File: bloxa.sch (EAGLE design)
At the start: 85 parts, among them CON1 PINHEAD_1X02-2.54, CON7 CON-4P-JST_GH-RA, CON8 CON-4P-JST_GH-RA, IC1 TPD3S014DBVR-SOT23-6, IC2 TJA1051(X)/3-SO8, IC6 MCP9700-SC70-5, Q13 BUK9K6R2-40E,115, Q14 BUK9K6R2-40E,115, Q15 BUK9K6R2-40E,115

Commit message: UPDATES
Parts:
- added U$1: CONNECTION, misc:CONNECTION
- added U$8, U$9: FIDUCIALMOUNT, usb2can_master_lib:FIDUCIALMOUNT
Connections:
- net GNDD: now also U$1.P$2
- net PGND: now also U$1.P$1
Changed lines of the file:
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@@
 <variantdefs>
 <variantdef name="Basic"/>
-<variantdef name="nocaps" current="yes"/>
+<variantdef name="nocaps"/>
 </variantdefs>
 <classes>
@@
 <part name="GND6" library="supply_symbols" library_urn="urn:adsk.eagle:library:5017758" deviceset="PGND" device="" value="PGND"/>
 <part name="C1" library="C_digikey" library_urn="urn:adsk.eagle:library:2539367" deviceset="0.1µF" device="-0402" package3d_urn="urn:adsk.eagle:package:2539379/2" technology="-16V_10%_X7R" value="0.1µF"/>
+<part name="U$1" library="misc" library_urn="urn:adsk.eagle:library:5347860" deviceset="CONNECTION" device=""/>
+<part name="GND7" library="supply_symbols" library_urn="urn:adsk.eagle:library:5017758" deviceset="GNDD" device="" value="GNDD"/>
+<part name="GND8" library="supply_symbols" library_urn="urn:adsk.eagle:library:5017758" deviceset="PGND" device="" value="PGND"/>
+<part name="U$8" library="usb2can_master_lib" deviceset="FIDUCIALMOUNT" device="">
+<variant name="Basic" populate="no"/>
+</part>
+<part name="U$9" library="usb2can_master_lib" deviceset="FIDUCIALMOUNT" device="">
+<variant name="Basic" populate="no"/>
+</part>
 </parts>
 <sheets>
@@
 <attribute name="VOLTAGE" x="162.814" y="180.594" size="0.762" layer="96" rot="R270" align="bottom-center"/>
 </instance>
+<instance part="U$1" gate="G$1" x="337.82" y="144.78" smashed="yes"/>
+<instance part="GND7" gate="G$1" x="342.9" y="139.7" smashed="yes">
+<attribute name="VALUE" x="342.9" y="137.668" size="1.27" layer="96" font="vector" ratio="15" align="center"/>
+</instance>
+<instance part="GND8" gate="G$1" x="332.74" y="139.7" smashed="yes" rot="MR0">
+<attribute name="VALUE" x="332.74" y="138.43" size="1.27" layer="97" font="vector" ratio="15" rot="MR0" align="center"/>
+</instance>
+<instance part="U$8" gate="G$1" x="25.4" y="12.7" smashed="yes" rot="R270"/>
+<instance part="U$9" gate="G$1" x="15.24" y="22.86" smashed="yes" rot="R270"/>
 </instances>
 <busses>
@@
 <wire x1="345.44" y1="71.12" x2="345.44" y2="73.66" width="0.1524" layer="91"/>
 <pinref part="GND19" gate="G$1" pin="GNDD"/>
+</segment>
+<segment>
+<pinref part="GND7" gate="G$1" pin="GNDD"/>
+<wire x1="342.9" y1="142.24" x2="342.9" y2="144.78" width="0.1524" layer="91"/>
+<pinref part="U$1" gate="G$1" pin="P$2"/>
+<wire x1="342.9" y1="144.78" x2="340.36" y2="144.78" width="0.1524" layer="91"/>
 </segment>
 </net>
@@
 <pinref part="GND6" gate="G$1" pin="PGND"/>
 </segment>
-</net>
+<segment>
+<pinref part="GND8" gate="G$1" pin="PGND"/>
+<wire x1="332.74" y1="142.24" x2="332.74" y2="144.78" width="0.1524" layer="91"/>
+<pinref part="U$1" gate="G$1" pin="P$1"/>
+<wire x1="332.74" y1="144.78" x2="335.28" y2="144.78" width="0.1524" layer="91"/>
+</segment>
+</net>

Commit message: More polygones updates
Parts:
- added U$3: CONNECTION, misc:CONNECTION
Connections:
- net GND: now also C1.2, C11.2, C3.2, CON1.1, IC2.GND, U$1.P$1, U$3.P$1
- net PGND: now also U$3.P$2; no longer C1.2, C11.2, C3.2, CON1.1, IC2.GND, U$1.P$1
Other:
- moved on the sheet: CON8, LED1, LED3, R11, R12, R13, R9

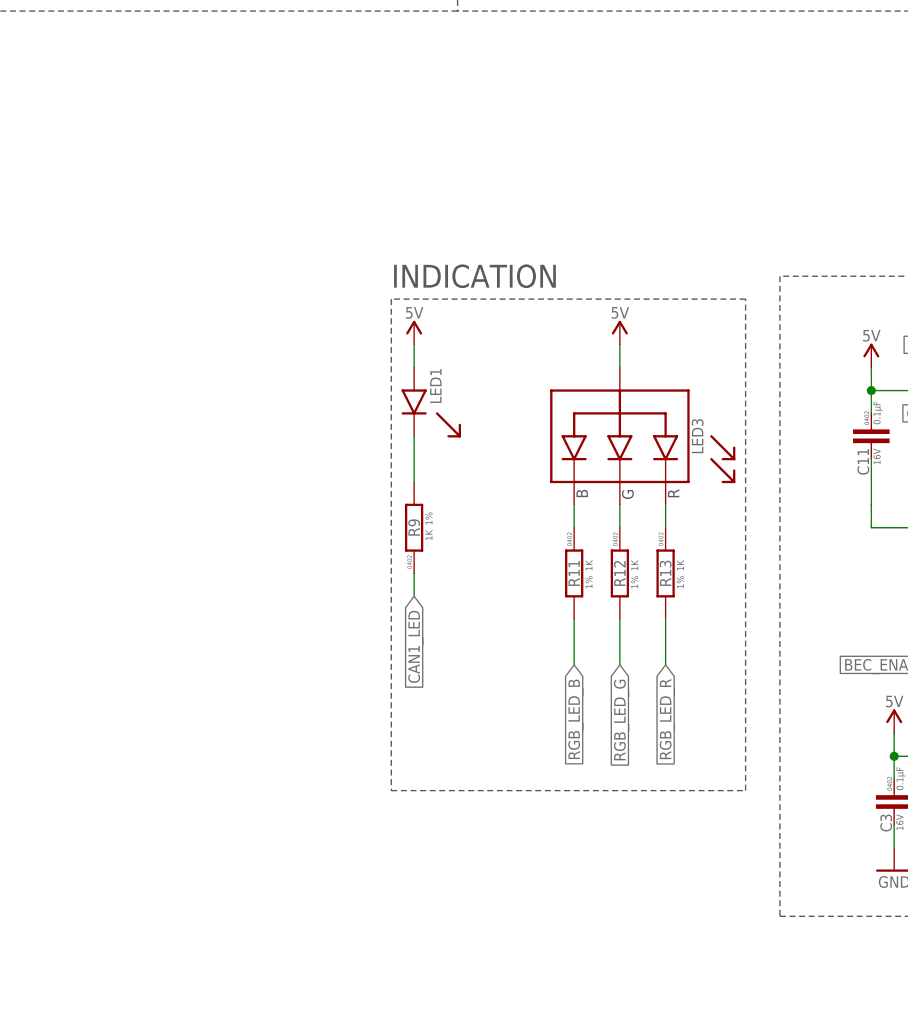
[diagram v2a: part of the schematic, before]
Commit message: alternate footprints for LED fancy placement
Will never use it probably
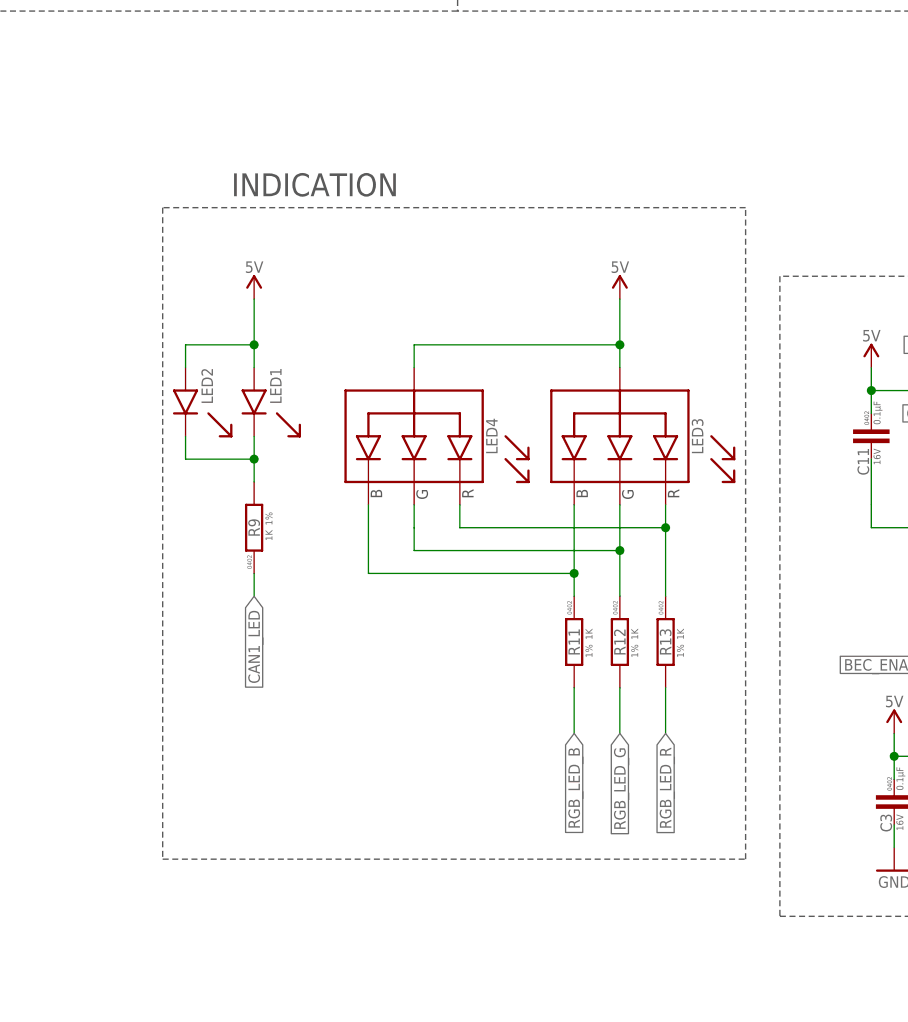
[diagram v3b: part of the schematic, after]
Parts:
- added LED2: GREEN, myxa_masterlib:LED-GREEN-0402
- added LED4: LTST-C19HE1WT, myxa_masterlib:LTST-C19HE1WT
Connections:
- removed net N$59: LED3.G, R12.1
- new net N$4: LED3.G, LED4.G, R12.1
- net N$17: now also LED2.C
- net N$58: now also LED4.R
- net N$60: now also LED4.B
- net VDD_5V: now also LED2.A, LED4.A
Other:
- moved on the sheet: LED1, R11, R12, R13, R9

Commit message: Renaming
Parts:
- removed C100, C102: 180µF, rc:CPOL-RADIAL_SIDE-8X21.5
- removed C15: 0.1µF, C_digikey:0.1µF-16V_10%_X7R-0402
- removed C16, C18: 10µF, C_digikey:10µF-50_10%_X7S-C1210
- removed CON7: CON-4P-JST_GH-RA, Connectors:CON-4P-JST_GH-RA
- removed IC6: MCP9700-SC70-5, misc:MCP9700-SC70-5
- removed R35, R36, R37: 4R3, R_digikey:4R3-5%-0402
- removed U$8, U$9: FIDUCIALMOUNT, usb2can_master_lib:FIDUCIALMOUNT
- added C10, C4: 0.1µF, C_digikey:0.1µF-16V_10%_X7R-0402
- added C12, C13, C14: 4.7µF, C_digikey:4.7µF-25V_10%_X6S-0603
- added CON3: PINHEAD_1X02-2.54, pinhead:PINHEAD_1X02-2.54
- added FD1, FD2: FIDUCIALMOUNT, misc:FIDUCIALMOUNT
- added IC3: TJA1051(X)/3-SO8, serial_interfaces:TJA1051(X)/3-SO8
- added R3, R5, R6: 1K, R_digikey:1K-1%-0402
- C1, C3: value 0.1µF -> 180µF; device C_digikey:0.1µF-16V_10%_X7R-0402 -> rc:CPOL-RADIAL_SIDE-8X21.5
- C5: value 4.7µF -> 0.1µF; device C_digikey:4.7µF-25V_10%_X6S-0603 -> C_digikey:0.1µF-16V_10%_X7R-0402
- C7, C9: value 4.7µF -> 10µF; device C_digikey:4.7µF-25V_10%_X6S-0603 -> C_digikey:10µF-50_10%_X7S-C1210
- CON1: value PINHEAD_1X02-2.54 -> CON-4P-JST_GH-RA; device pinhead:PINHEAD_1X02-2.54 -> Connectors:CON-4P-JST_GH-RA
- IC1: value TPD3S014DBVR-SOT23-6 -> MCP9700-SC70-5; device myxa_masterlib:TPD3S014DBVR-SOT23-6 -> misc:MCP9700-SC70-5
- IC2: value TJA1051(X)/3-SO8 -> TPD3S014DBVR-SOT23-6; device serial_interfaces:TJA1051(X)/3-SO8 -> myxa_masterlib:TPD3S014DBVR-SOT23-6
- PAD22, PAD23, PAD24, PAD4: value PAD-HOLE-0.6 -> PAD-1X1.5; device PADS:PAD-HOLE-0.6 -> PADS:PAD-1X1.5
- PAD38, PAD39, PAD40, PAD41: value PAD-1X1.5 -> PAD-HOLE-0.6; device PADS:PAD-1X1.5 -> PADS:PAD-HOLE-0.6
- R11, R12, R9: value 1K -> 4R3; device R_digikey:1K-1%-0402 -> R_digikey:4R3-5%-0402
- renumbered A to PAD44, B to PAD45, BAT+ to PAD42, BAT- to PAD43, C to PAD46, C101 to C2, C17 to C8, C21 to C6, CON8 to CON2, D2 to D1, Q13 to Q1, Q14 to Q2, Q15 to Q3, R13 to R7, R26 to R4, R31 to R1, R32 to R2, R33 to R10, R34 to R8, S2 to S1, U$1 to J2, U$3 to J1
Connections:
- net BEC_ENABLE_OUT: now also IC2.EN, PAD21.P$1; no longer IC1.EN, PAD24.P$1
- net CAN1_LED: now also PAD6.P$1, R3.1; no longer PAD36.P$1, R9.1
- net CAN1_RX: now also IC3.RXD, PAD2.P$1; no longer IC2.RXD, PAD40.P$1
- net CAN1_TX: now also IC3.TXD, PAD1.P$1; no longer IC2.TXD, PAD41.P$1
- net CAN1_VDD: now also C12.2, C13.2, C14.2, CON1.1, IC2.OUT; no longer C5.2, C7.2, C9.2, CON7.1, IC1.OUT
- net CAN2_LED: now also PAD5.P$1; no longer PAD37.P$1
- net CAN2_RX: now also PAD4.P$1; no longer PAD38.P$1
- net CAN2_TX: now also PAD3.P$1; no longer PAD39.P$1
- net EN_GATE_OUT: now also PAD16.P$1; no longer PAD26.P$1
- net GAIN_OUT: now also PAD17.P$1; no longer PAD25.P$1
- net GND: now also C10.2, C4.2, CON3.1, IC3.GND; no longer C1.2, C3.2, CON1.1, IC1.GND
- net GNDD: now also C12.1, C13.1, C14.1, CON1.4, CON1.GND; no longer C5.1, C7.1, C9.1, CON7.4, CON7.GND
- net GPIO1: now also CON3.2, PAD14.P$1; no longer CON1.2, PAD28.P$1
- net GPIO2: now also PAD15.P$1; no longer PAD27.P$1
- net N$17: now also R3.2; no longer R9.2
- net N$2: now also IC3.S; no longer IC2.S
- net N$22: now also CON1.2, IC3.CANH; no longer CON7.2, IC2.CANH
- net N$23: now also CON1.3, IC3.CANL; no longer CON7.3, IC2.CANL
- net N$28: now also R11.2; no longer R36.2
- net N$29: now also R12.2; no longer R37.2
- net N$31: now also R9.2; no longer R35.2
- net N$4: now also R6.1; no longer R12.1
- net N$60: now also R5.1; no longer R11.1
- net OVERCURRENT_PROTECT_ADJ: now also PAD13.P$1; no longer PAD29.P$1
- net PGND: now also C1.-, C3.-, C5.2, C7.1, C9.1, IC1.GND, PAD23.P$1; no longer C100.-, C102.-, C15.2, C16.1, C18.1, IC6.GND, PAD2.P$1
- net PHASE_A: now also PAD26.P$1; no longer PAD5.P$1
- net PHASE_A_CURRENT_SHUNT_N: now also PAD37.P$1; no longer PAD16.P$1
- net PHASE_A_CURRENT_SHUNT_P: now also PAD38.P$1; no longer PAD17.P$1
- net PHASE_A_GATE_HIGH: now also PAD25.P$1; no longer PAD4.P$1
- net PHASE_A_GATE_LOW: now also PAD27.P$1; no longer PAD6.P$1
- net PHASE_A_GND: now also PAD28.P$1; no longer PAD7.P$1
- net PHASE_B: now also PAD30.P$1; no longer PAD9.P$1
- net PHASE_B_CURRENT_SHUNT_N: now also PAD39.P$1; no longer PAD18.P$1
- net PHASE_B_CURRENT_SHUNT_P: now also PAD40.P$1; no longer PAD19.P$1
- net PHASE_B_GATE_HIGH: now also PAD29.P$1; no longer PAD8.P$1
- net PHASE_B_GATE_LOW: now also PAD31.P$1, R9.1; no longer PAD10.P$1, R35.1
- net PHASE_B_GND: now also PAD32.P$1; no longer PAD11.P$1
- net PHASE_C: now also PAD34.P$1; no longer PAD13.P$1
- net PHASE_C_GATE_HIGH: now also PAD33.P$1, R11.1; no longer PAD12.P$1, R36.1
- net PHASE_C_GATE_LOW: now also PAD35.P$1, R12.1; no longer PAD14.P$1, R37.1
- net PHASE_C_GND: now also PAD36.P$1; no longer PAD15.P$1
- net POWER_ENABLE_IN: now also PAD18.P$1; no longer PAD21.P$1
- net RGB_LED_B: now also PAD10.P$1, R5.2; no longer PAD32.P$1, R11.2
- net RGB_LED_G: now also PAD11.P$1, R6.2; no longer PAD31.P$1, R12.2
- net RGB_LED_R: now also PAD12.P$1; no longer PAD30.P$1
- net TEMPERATURE_SENSOR: now also C4.1, IC1.OUT, PAD41.P$1; no longer C1.1, IC6.OUT, PAD20.P$1
- net USART_RX: now also PAD20.P$1; no longer PAD23.P$1
- net USART_TX: now also PAD19.P$1; no longer PAD22.P$1
- net USB+: now also PAD7.P$1; no longer PAD35.P$1
- net USB-: now also PAD8.P$1; no longer PAD34.P$1
- net USB_VBUS: now also PAD9.P$1; no longer PAD33.P$1
- net VDC: now also C1.+, C3.+, C7.2, C9.2, PAD24.P$1; no longer C100.+, C102.+, C16.2, C18.2, PAD3.P$1
- net VDD_5V: now also C10.1, C5.1, IC1.VCC, IC2.IN, IC3.VCC, IC3.VIO, PAD22.P$1; no longer C15.1, C3.1, IC1.IN, IC2.VCC, IC2.VIO, IC6.VCC, PAD1.P$1
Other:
- moved on the sheet: C11, C5, C7, C9, LED1, LED2, LED3, LED4, PAD1, PAD10, PAD11, PAD12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

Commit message: gerber files added
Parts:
- R10, R4: value 3 mOhms -> 5 mOhms; device SHUNT_RESISTORS:CURRENT_SHUNT_KELVIN-0.003R-2512-KELVIN -> SHUNT_RESISTORS:CURRENT_SHUNT_KELVIN-0.005R-2512-KELVIN
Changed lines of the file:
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@@
 </attributes>
 <variantdefs>
-<variantdef name="Basic" current="yes"/>
+<variantdef name="Basic"/>
 <variantdef name="nocaps"/>
 </variantdefs>
@@
 <variant name="Basic" populate="no"/>
 </part>
-<part name="R4" library="SHUNT_RESISTORS" library_urn="urn:adsk.eagle:library:2644450" deviceset="CURRENT_SHUNT_KELVIN" device="-2512-KELVIN" package3d_urn="urn:adsk.eagle:package:3560627/3" technology="-0.003R" value="3 mOhms"/>
+<part name="R4" library="SHUNT_RESISTORS" library_urn="urn:adsk.eagle:library:2644450" deviceset="CURRENT_SHUNT_KELVIN" device="-2512-KELVIN" package3d_urn="urn:adsk.eagle:package:3560627/3" technology="-0.005R" value="5 mOhms"/>
 <part name="IC1" library="misc" library_urn="urn:adsk.eagle:library:5347860" deviceset="MCP9700" device="-SC70-5" package3d_urn="urn:adsk.eagle:package:7365869/3"/>
 <part name="C5" library="C_digikey" library_urn="urn:adsk.eagle:library:2539367" deviceset="0.1µF" device="-0402" package3d_urn="urn:adsk.eagle:package:2539379/2" technology="-16V_10%_X7R" value="0.1µF"/>
@@
 <variant name="Basic" populate="no"/>
 </part>
-<part name="R10" library="SHUNT_RESISTORS" library_urn="urn:adsk.eagle:library:2644450" deviceset="CURRENT_SHUNT_KELVIN" device="-2512-KELVIN" package3d_urn="urn:adsk.eagle:package:3560627/3" technology="-0.003R" value="3 mOhms"/>
+<part name="R10" library="SHUNT_RESISTORS" library_urn="urn:adsk.eagle:library:2644450" deviceset="CURRENT_SHUNT_KELVIN" device="-2512-KELVIN" package3d_urn="urn:adsk.eagle:package:3560627/3" technology="-0.005R" value="5 mOhms"/>
 <part name="R8" library="R_digikey" library_urn="urn:adsk.eagle:library:2539499" deviceset="4R3" device="-0402" package3d_urn="urn:adsk.eagle:package:2539512/2" technology="-5%" value="4R3"/>
 <part name="R9" library="R_digikey" library_urn="urn:adsk.eagle:library:2539499" deviceset="4R3" device="-0402" package3d_urn="urn:adsk.eagle:package:2539512/2" technology="-5%" value="4R3"/>
@@
 <part name="S1" library="misc" library_urn="urn:adsk.eagle:library:5347860" deviceset="SENSE" device="" package3d_urn="urn:adsk.eagle:package:7365871/1">
 <variant name="Basic" populate="no"/>
+<variant name="nocaps" populate="no"/>
 </part>
 <part name="C7" library="C_digikey" library_urn="urn:adsk.eagle:library:2539367" deviceset="10µF" device="-C1210" package3d_urn="urn:adsk.eagle:package:2539380/2" technology="-50_10%_X7S" value="10µF"/>
@@
 <part name="D1" library="TVS_diodes" library_urn="urn:adsk.eagle:library:3333632" deviceset="PTVS36VP1UP,115" device="-SOD128" package3d_urn="urn:adsk.eagle:package:6533206/2" technology="-36V"/>
 <part name="C1" library="rc" library_urn="urn:adsk.eagle:library:2539423" deviceset="CPOL" device="-RADIAL_SIDE-8X21.5" package3d_urn="urn:adsk.eagle:package:7189333/3" value="180µF">
-<variant name="Basic" populate="no"/>
 <variant name="nocaps" populate="no"/>
 </part>
 <part name="C3" library="rc" library_urn="urn:adsk.eagle:library:2539423" deviceset="CPOL" device="-RADIAL_SIDE-8X21.5" package3d_urn="urn:adsk.eagle:package:7189333/3" value="180µF">
-<variant name="Basic" populate="no"/>
 <variant name="nocaps" populate="no"/>
 </part>
@@
 <part name="+P5" library="supply_symbols" library_urn="urn:adsk.eagle:library:5017758" deviceset="VDC" device=""/>
 <part name="C2" library="rc" library_urn="urn:adsk.eagle:library:2539423" deviceset="CPOL" device="-RADIAL_SIDE-8X21.5" package3d_urn="urn:adsk.eagle:package:7189333/3" value="180µF">
-<variant name="Basic" populate="no"/>
 <variant name="nocaps" populate="no"/>
 </part>
@@
 <part name="GND1" library="supply_symbols" library_urn="urn:adsk.eagle:library:5017758" deviceset="PGND" device="" value="PGND"/>
 <part name="C4" library="C_digikey" library_urn="urn:adsk.eagle:library:2539367" deviceset="0.1µF" device="-0402" package3d_urn="urn:adsk.eagle:package:2539379/2" technology="-16V_10%_X7R" value="0.1µF"/>
-<part name="J2" library="misc" library_urn="urn:adsk.eagle:library:5347860" deviceset="CONNECTION" device="" package3d_urn="urn:adsk.eagle:package:7439847/1"/>
+<part name="J2" library="misc" library_urn="urn:adsk.eagle:library:5347860" deviceset="CONNECTION" device="" package3d_urn="urn:adsk.eagle:package:7439847/1">
+<variant name="Basic" populate="no"/>
+<variant name="nocaps" populate="no"/>
+</part>
 <part name="GND18" library="supply_symbols" library_urn="urn:adsk.eagle:library:5017758" deviceset="GNDD" device="" value="GNDD"/>
 <part name="FD2" library="misc" library_urn="urn:adsk.eagle:library:5347860" deviceset="FIDUCIALMOUNT" device="">
@@
 <variant name="Basic" populate="no"/>
 </part>
-<part name="J1" library="misc" library_urn="urn:adsk.eagle:library:5347860" deviceset="CONNECTION" device="" package3d_urn="urn:adsk.eagle:package:7439847/1"/>
+<part name="J1" library="misc" library_urn="urn:adsk.eagle:library:5347860" deviceset="CONNECTION" device="" package3d_urn="urn:adsk.eagle:package:7439847/1">
+<variant name="Basic" populate="no"/>
+<variant name="nocaps" populate="no"/>
+</part>
 <part name="GND13" library="supply_symbols" library_urn="urn:adsk.eagle:library:5017758" deviceset="PGND" device="" value="PGND"/>
 <part name="GND15" library="supply_symbols" library_urn="urn:adsk.eagle:library:5017758" deviceset="GND" device="" value="GND"/>

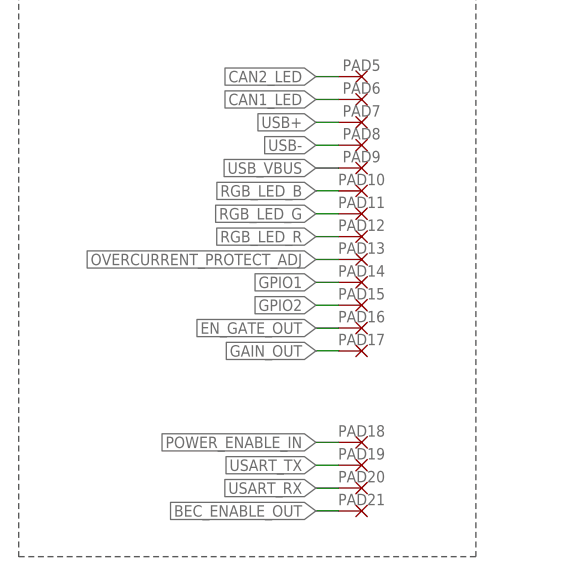
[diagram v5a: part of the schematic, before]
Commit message: OC_ADJ resistor added
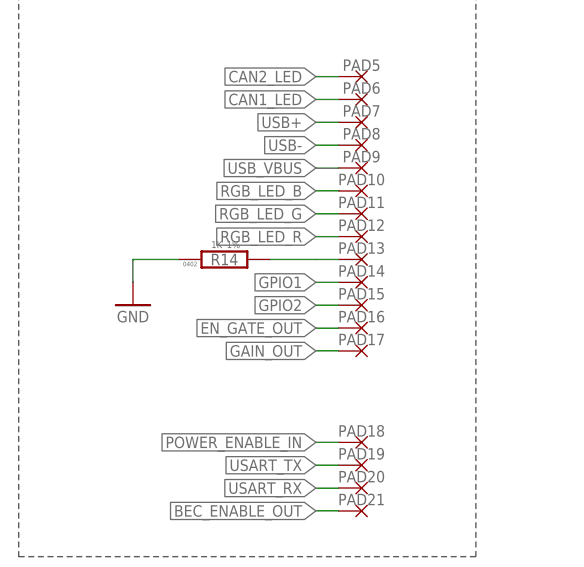
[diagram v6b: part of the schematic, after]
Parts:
- added R14: 1K, R_digikey:1K-1%-0402
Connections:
- net GND: now also R14.1
- net OVERCURRENT_PROTECT_ADJ: now also R14.2
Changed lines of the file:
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@@
 <?xml version="1.0" encoding="utf-8"?>
 <!DOCTYPE eagle SYSTEM "eagle.dtd">
-<eagle version="9.2.2">
+<eagle version="9.3.0">
 <drawing>
 <settings>
@@
 <variant name="Basic" populate="no"/>
 </part>
+<part name="R14" library="R_digikey" library_urn="urn:adsk.eagle:library:2539499" deviceset="1K" device="-0402" package3d_urn="urn:adsk.eagle:package:2539512/2" technology="-1%" value="1K"/>
+<part name="GND25" library="supply_symbols" library_urn="urn:adsk.eagle:library:5017758" deviceset="GND" device="" value="GND"/>
 </parts>
 <sheets>
@@
 <attribute name="NAME" x="257.556" y="116.84" size="1.27" layer="95" font="vector" ratio="15" rot="R270" align="center"/>
 </instance>
+<instance part="R14" gate="G$1" x="33.02" y="116.84" smashed="yes" rot="MR180">
+<attribute name="NAME" x="33.02" y="116.84" size="1.27" layer="95" rot="MR180" align="center"/>
+<attribute name="VALUE" x="32.766" y="118.872" size="0.762" layer="96" rot="MR180" align="bottom-right"/>
+<attribute name="PACKAGE" x="29.21" y="116.332" size="0.508" layer="95" rot="MR180" align="center"/>
+<attribute name="TOLERANCE" x="33.274" y="118.872" size="0.762" layer="96" rot="MR180"/>
+</instance>
+<instance part="GND25" gate="1" x="22.86" y="111.76" smashed="yes">
+<attribute name="VALUE" x="22.86" y="110.49" size="1.27" layer="96" font="vector" ratio="15" align="center"/>
+</instance>
 </instances>
 <busses>
@@
 <segment>
 <wire x1="45.72" y1="116.84" x2="43.18" y2="116.84" width="0.1524" layer="91"/>
-<label x="43.18" y="116.84" size="1.27" layer="95" rot="R180" xref="yes"/>
 <pinref part="PAD13" gate="G$1" pin="P$1"/>
+<wire x1="43.18" y1="116.84" x2="38.1" y2="116.84" width="0.1524" layer="91"/>
+<pinref part="R14" gate="G$1" pin="2"/>
 </segment>
 </net>
@@
 <wire x1="162.56" y1="175.26" x2="162.56" y2="177.8" width="0.1524" layer="91"/>
 </segment>
-</net>
+<segment>
+<wire x1="22.86" y1="114.3" x2="22.86" y2="116.84" width="0.1524" layer="91"/>
+<wire x1="22.86" y1="116.84" x2="27.94" y2="116.84" width="0.1524" layer="91"/>
+<pinref part="R14" gate="G$1" pin="1"/>
+<pinref part="GND25" gate="1" pin="GND"/>
+</segment>
+</net>
